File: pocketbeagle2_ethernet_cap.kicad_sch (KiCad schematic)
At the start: 1 part, among them U1 PocketBeagle2

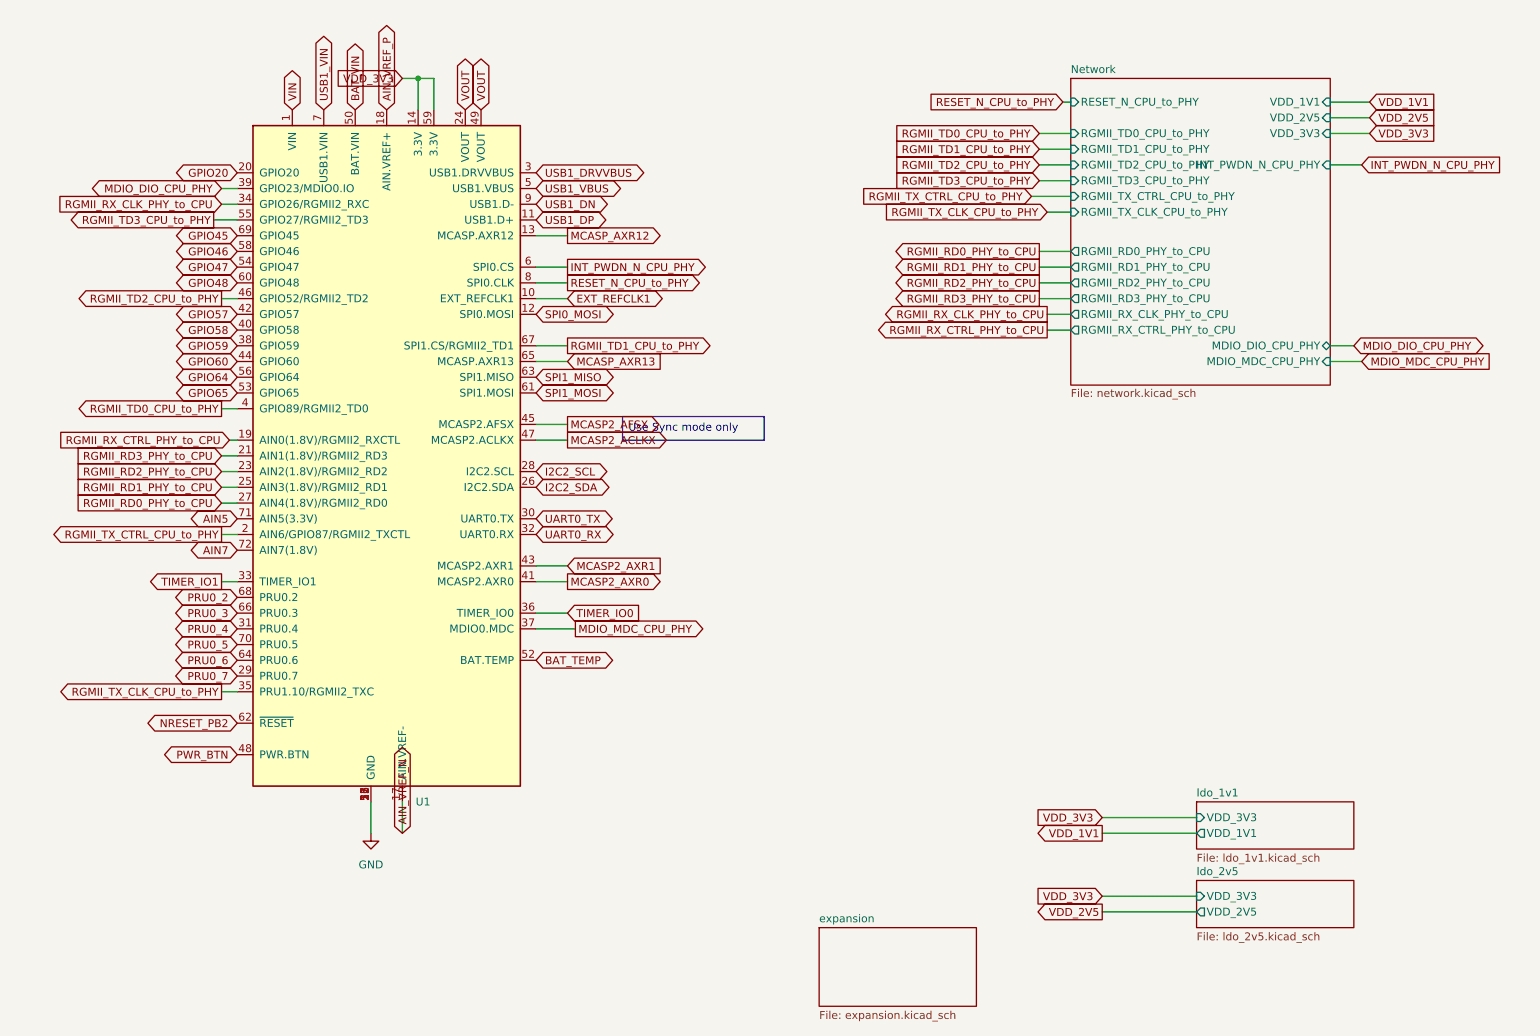
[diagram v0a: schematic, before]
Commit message: Convert to hierarchical port design, move PocketBeagle into io sheet
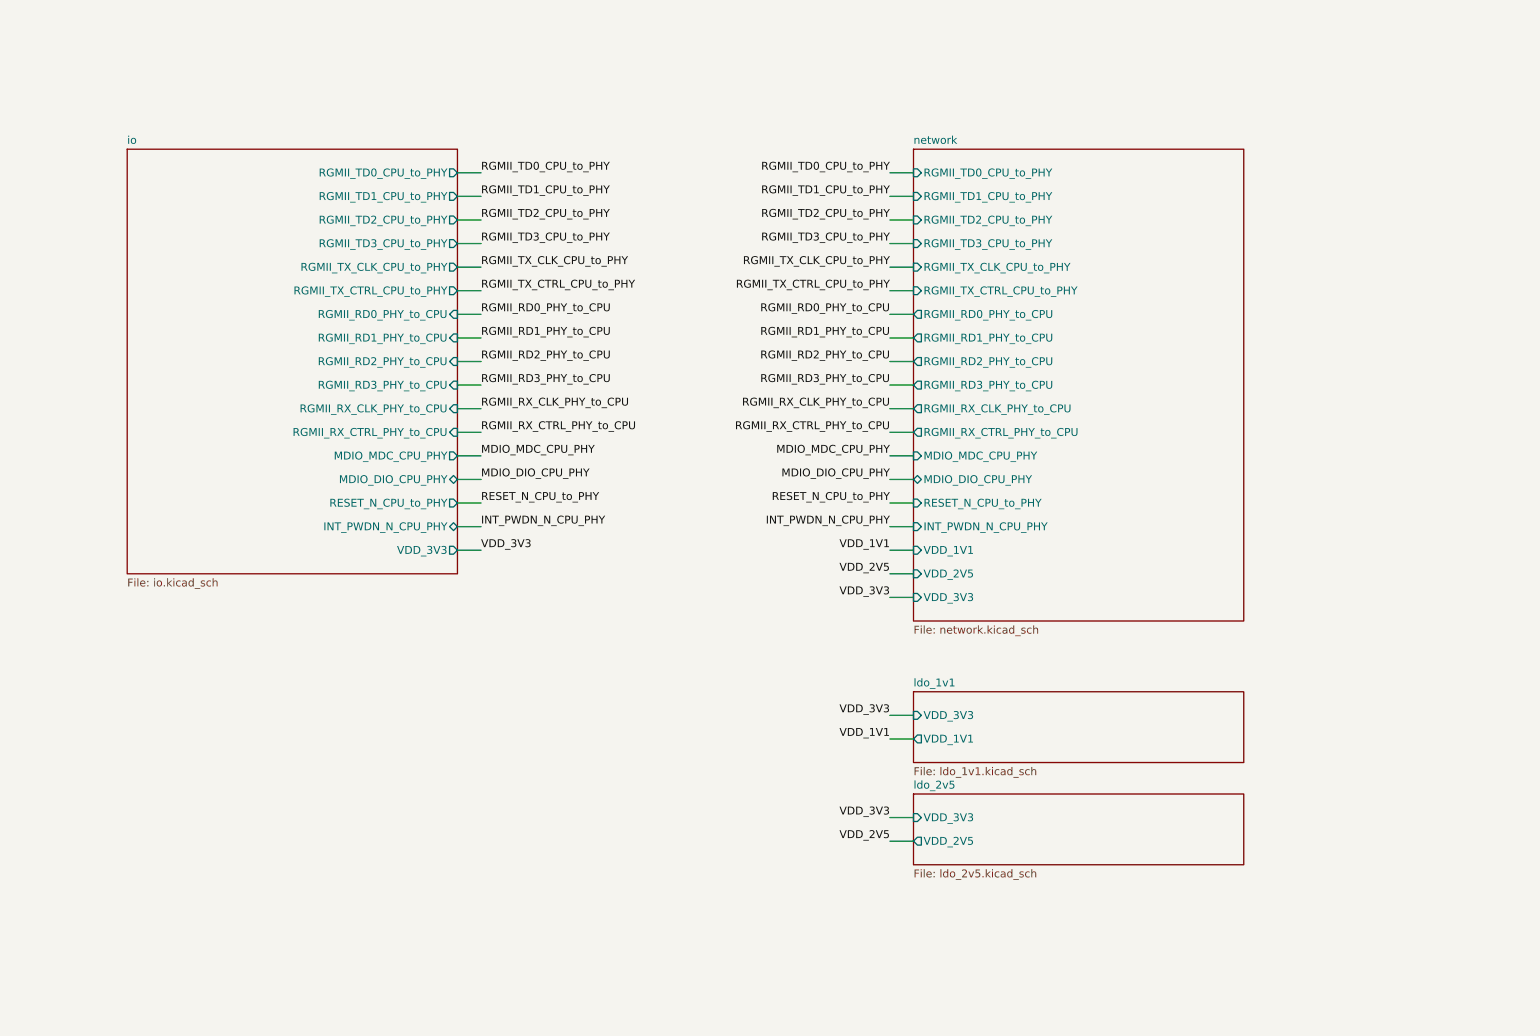
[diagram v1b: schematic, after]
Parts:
- removed U1: PocketBeagle2, KL_Footprints:BeagleBoard_PocketBeagle, symbol KL_Module:PocketBeagle2
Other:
- sheet Network renamed network
- sheet expansion renamed io
- sheet io: file expansion.kicad_sch -> io.kicad_sch
- sheet io ports: added INT_PWDN_N_CPU_PHY, MDIO_DIO_CPU_PHY, MDIO_MDC_CPU_PHY, RESET_N_CPU_to_PHY, RGMII_RD0_PHY_to_CPU, RGMII_RD1_PHY_to_CPU, RGMII_RD2_PHY_to_CPU, RGMII_RD3_PHY_to_CPU, RGMII_RX_CLK_PHY_to_CPU, RGMII_RX_CTRL_PHY_to_CPU, RGMII_TD0_CPU_to_PHY, RGMII_TD1_CPU_to_PHY, RGMII_TD2_CPU_to_PHY, RGMII_TD3_CPU_to_PHY, RGMII_TX_CLK_CPU_to_PHY, RGMII_TX_CTRL_CPU_to_PHY, VDD_3V3; removed none
